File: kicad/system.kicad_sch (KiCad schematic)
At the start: 6 parts

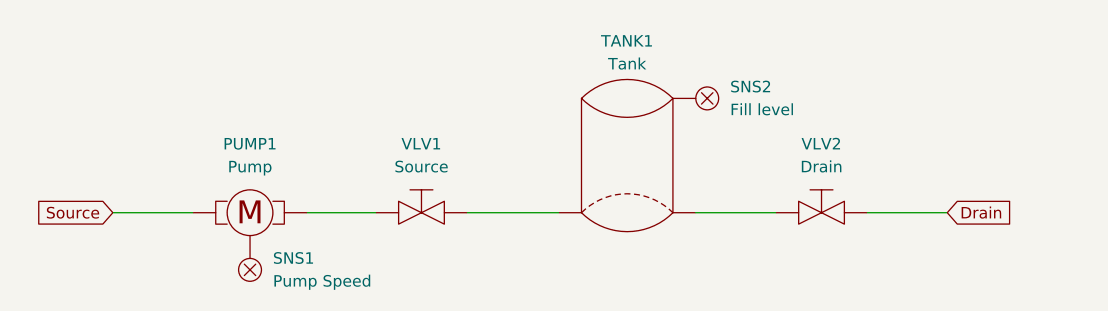
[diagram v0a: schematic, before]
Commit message: Fix bugs in diagrams.
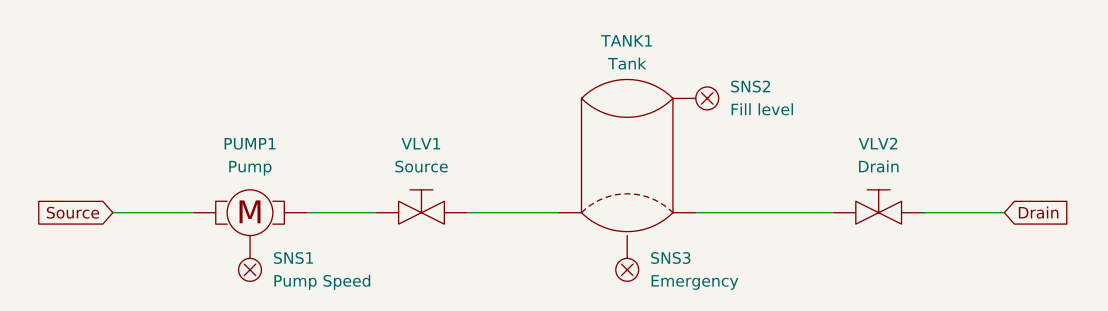
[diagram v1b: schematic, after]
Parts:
- added SNS3: Emergency, symbol pico-rio:Sensor
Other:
- moved on the sheet: VLV2
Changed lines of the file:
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@@
 	(wire
 		(pts
-			(xy 180.34 99.06) (xy 189.23 99.06)
+			(xy 186.69 99.06) (xy 195.58 99.06)
 		)
 		(stroke
@@
 	(wire
 		(pts
-			(xy 170.18 99.06) (xy 161.29 99.06)
+			(xy 176.53 99.06) (xy 161.29 99.06)
 		)
 		(stroke
@@
 	(global_label "Drain"
 		(shape input)
-		(at 189.23 99.06 0)
+		(at 195.58 99.06 0)
 		(fields_autoplaced yes)
 		(effects
@@
 		)
 		(property "Intersheetrefs" "${INTERSHEET_REFS}"
-			(at 197.1742 99.06 0)
+			(at 203.5242 99.06 0)
 			(effects
 				(font
@@
 	)
 	(symbol
+		(lib_id "pico-rio:Sensor")
+		(at 153.67 105.41 180)
+		(unit 1)
+		(exclude_from_sim no)
+		(in_bom yes)
+		(on_board yes)
+		(dnp no)
+		(fields_autoplaced yes)
+		(property "Reference" "SNS3"
+			(at 156.21 104.1399 0)
+			(effects
+				(font
+					(size 1.27 1.27)
+				)
+				(justify right)
+			)
+		)
+		(property "Value" "Emergency"
+			(at 156.21 106.6799 0)
+			(effects
+				(font
+					(size 1.27 1.27)
+				)
+				(justify right)
+			)
+		)
+		(property "Footprint" ""
+			(at 153.67 105.41 0)
+			(effects
+				(font
+					(size 1.27 1.27)
+				)
+				(hide yes)
+			)
+		)
+		(property "Datasheet" ""
+			(at 153.67 105.41 0)
+			(effects
+				(font
+					(size 1.27 1.27)
+				)
+				(hide yes)
+			)
+		)
+		(property "Description" ""
+			(at 153.67 105.41 0)
+			(effects
+				(font
+					(size 1.27 1.27)
+				)
+				(hide yes)
+			)
+		)
+		(pin "1"
+		)
+		(instances
+			(project "system"
+				(path "/9b126da4-a818-4f6e-b5fc-eb980603cbf8"
+					(reference "SNS3")
+					(unit 1)
+				)
+			)
+		)
+	)
+	(symbol
 		(lib_id "pico-rio:Valve")
-		(at 175.26 99.06 0)
+		(at 181.61 99.06 0)
 		(unit 1)
 		(exclude_from_sim no)
@@
 		(fields_autoplaced yes)
 		(property "Reference" "VLV2"
-			(at 175.26 91.44 0)
+			(at 181.61 91.44 0)
 			(effects
 				(font
@@
 		)
 		(property "Value" "Drain"
-			(at 175.26 93.98 0)
-			(effects
-				(font
-					(size 1.27 1.27)
-				)
-			)
-		)
-		(property "Footprint" ""
-			(at 175.26 99.06 0)
-			(effects
-				(font
-					(size 1.27 1.27)
-				)
-				(hide yes)
-			)
-		)
-		(property "Datasheet" ""
-			(at 175.26 99.06 0)
-			(effects
-				(font
-					(size 1.27 1.27)
-				)
-				(hide yes)
-			)
-		)
-		(property "Description" ""
-			(at 175.26 99.06 0)
-			(effects
-				(font
+			(at 181.61 93.98 0)
+			(effects
+				(font
+					(size 1.27 1.27)
+				)
+			)
+		)
+		(property "Footprint" ""
+			(at 181.61 99.06 0)
+			(effects
+				(font
+					(size 1.27 1.27)
+				)
+				(hide yes)
+			)
+		)
+		(property "Datasheet" ""
+			(at 181.61 99.06 0)
+			(effects
+				(font
+					(size 1.27 1.27)
+				)
+				(hide yes)
+			)
+		)
+		(property "Description" ""
+			(at 181.61 99.06 0)
+			(effects
+				(font

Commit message: Update README and diagrams.
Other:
- moved on the sheet: PUMP1, SNS1, VLV1
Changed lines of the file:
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@@
 	(wire
 		(pts
-			(xy 96.52 99.06) (xy 105.41 99.06)
-		)
-		(stroke
-			(width 0)
-			(type default)
-		)
-	)
-	(wire
-		(pts
-			(xy 135.89 99.06) (xy 146.05 99.06)
+			(xy 96.52 86.36) (xy 105.41 86.36)
+		)
+		(stroke
+			(width 0)
+			(type default)
+		)
+	)
+	(wire
+		(pts
+			(xy 135.89 86.36) (xy 146.05 86.36)
 		)
 		(stroke
@@
 	(wire
 		(pts
-			(xy 118.11 99.06) (xy 125.73 99.06)
+			(xy 118.11 86.36) (xy 125.73 86.36)
 		)
 		(stroke
@@
 	(global_label "Source"
 		(shape input)
-		(at 96.52 99.06 180)
+		(at 96.52 86.36 180)
 		(fields_autoplaced yes)
 		(effects
@@
 		)
 		(property "Intersheetrefs" "${INTERSHEET_REFS}"
-			(at 87.0639 99.06 0)
+			(at 87.0639 86.36 0)
 			(effects
 				(font
@@
 	(symbol
 		(lib_id "pico-rio:Sensor")
-		(at 111.76 105.41 180)
+		(at 111.76 92.71 180)
 		(unit 1)
 		(exclude_from_sim no)
@@
 		(fields_autoplaced yes)
 		(property "Reference" "SNS1"
-			(at 114.3 104.1399 0)
+			(at 114.3 91.4399 0)
 			(effects
 				(font
@@
 		)
 		(property "Value" "Pump Speed"
-			(at 114.3 106.6799 0)
+			(at 114.3 93.9799 0)
 			(effects
 				(font
@@
 		)
 		(property "Footprint" ""
-			(at 111.76 105.41 0)
+			(at 111.76 92.71 0)
 			(effects
 				(font
@@
 		)
 		(property "Datasheet" ""
-			(at 111.76 105.41 0)
+			(at 111.76 92.71 0)
 			(effects
 				(font
@@
 		)
 		(property "Description" ""
-			(at 111.76 105.41 0)
+			(at 111.76 92.71 0)
 			(effects
 				(font
@@
 	(symbol
 		(lib_id "pico-rio:Pump")
-		(at 111.76 99.06 0)
+		(at 111.76 86.36 0)
 		(unit 1)
 		(exclude_from_sim no)
@@
 		(fields_autoplaced yes)
 		(property "Reference" "PUMP1"
-			(at 111.76 91.44 0)
+			(at 111.76 78.74 0)
 			(effects
 				(font
@@
 		)
 		(property "Value" "Pump"
-			(at 111.76 93.98 0)
+			(at 111.76 81.28 0)
 			(effects
 				(font
@@
 		)
 		(property "Footprint" ""
-			(at 111.76 99.06 0)
+			(at 111.76 86.36 0)
 			(effects
 				(font
@@
 		)
 		(property "Datasheet" ""
-			(at 111.76 99.06 0)
+			(at 111.76 86.36 0)
 			(effects
 				(font
@@
 		)
 		(property "Description" ""
-			(at 111.76 99.06 0)
+			(at 111.76 86.36 0)
 			(effects
 				(font
@@
 	(symbol
 		(lib_id "pico-rio:Valve")
-		(at 130.81 99.06 0)
+		(at 130.81 86.36 0)
 		(unit 1)
 		(exclude_from_sim no)
@@
 		(fields_autoplaced yes)
 		(property "Reference" "VLV1"
-			(at 130.81 91.44 0)
+			(at 130.81 78.74 0)
 			(effects
 				(font
@@
 		)
 		(property "Value" "Source"
-			(at 130.81 93.98 0)
+			(at 130.81 81.28 0)
 			(effects
 				(font
@@
 		)
 		(property "Footprint" ""
-			(at 130.81 99.06 0)
+			(at 130.81 86.36 0)
 			(effects
 				(font
@@
 		)
 		(property "Datasheet" ""
-			(at 130.81 99.06 0)
+			(at 130.81 86.36 0)
 			(effects
 				(font
@@
 		)
 		(property "Description" ""
-			(at 130.81 99.06 0)
-			(effects
-				(font
+			(at 130.81 86.36 0)
+			(effects
+				(font
